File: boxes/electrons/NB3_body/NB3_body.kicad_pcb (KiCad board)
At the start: 2 copper layers, 200 x 199.5 mm, 21 parts, among them J1 Conn_01x02_Male, J2 Conn_01x02_Male, J3 Conn_01x02_Male, J4 Conn_01x02_Male, J5 Conn_01x04_Male, J6 Conn_01x02_Male

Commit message: Work on NB3_body PCB...
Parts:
- removed C3, C4, C5: 10uF, Capacitor_SMD:C_0805_2012Metric
- removed F3, F4, F6: 1.1h2.2t, Fuse:Fuse_0805_2012Metric
- removed F5: 3h5t, Fuse:Fuse_2920_7451Metric
- added J10: Conn_01x03_Female, Connector_PinHeader_2.54mm:PinHeader_1x03_P2.54mm_Vertical_SMD_Pin1Right, F.Cu at (107.5, 36.0)
- added J11: Conn_02x10_Odd_Even, Connector_PinHeader_2.54mm:PinHeader_2x10_P2.54mm_Vertical_SMD, F.Cu at (169.0, 58.5)
- added J12: Conn_01x04_Male, Connector_PinHeader_2.54mm:PinHeader_1x04_P2.54mm_Vertical_SMD_Pin1Right, F.Cu at (167.5, 74.0)
- added J7: Socket_SM06B-SRSS-TB, NB3_body:Socket_SM06B-SRSS-TB, F.Cu at (26.5, 195.0)
- added J8: Socket_SM06B-SRSS-TB, NB3_body:Socket_SM06B-SRSS-TB, F.Cu at (222.5, 196.0)
- added J9: Conn_01x03_Female, Connector_PinHeader_2.54mm:PinHeader_1x03_P2.54mm_Vertical_SMD_Pin1Right, F.Cu at (141.5, 36.0)
- J1, J2: value Conn_01x02_Male -> Conn_01x03_Female; footprint Connector_PinHeader_2.54mm:PinHeader_1x02_P2.54mm_Vertical_SMD_Pin1Right -> Connector_PinHeader_2.54mm:PinHeader_1x03_P2.54mm_Vertical_SMD_Pin1Right
- J3, J4, J6: value Conn_01x02_Male -> Conn_01x10_Male; footprint Connector_PinHeader_2.54mm:PinHeader_1x02_P2.54mm_Vertical_SMD_Pin1Right -> Connector_PinHeader_2.54mm:PinHeader_1x10_P2.54mm_Vertical_SMD_Pin1Right
- J5: value Conn_01x04_Male -> Conn_01x10_Male; footprint Connector_PinHeader_2.54mm:PinHeader_1x04_P2.54mm_Vertical_SMD_Pin1Right -> Connector_PinHeader_2.54mm:PinHeader_1x10_P2.54mm_Vertical_SMD_Pin1Right
- moved J2 127.7 mm to (163.5, 34.5), turned to 90 degrees
- moved J1 124.2 mm to (87.0, 34.0), turned to 90 degrees
- moved J3 86.6 mm to (67.5, 88.0), turned to 90 degrees
- moved H1 84.1 mm to (93.5, 58.0)
- moved C2 83.4 mm to (109.5, 71.5)
- moved J4 81.8 mm to (181.5, 88.0), turned to 90 degrees
- moved H2 79.8 mm to (136.5, 58.0)
- moved C1 78.1 mm to (117.5, 71.5)
- moved F1 73.2 mm to (117.5, 78.0)
- moved F2 72.2 mm to (109.5, 78.0)
- moved H3 62.2 mm to (93.5, 96.0)
- moved H4 52.8 mm to (136.5, 96.0)
- moved J5 43.0 mm to (76.5, 163.0), turned to 90 degrees
- moved J6 35.8 mm to (172.5, 163.0), turned to -90 degrees
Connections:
- C1 pad 1: +5V -> unconnected-(C1-Pad1)
- C1 pad 2: GND -> unconnected-(C1-Pad2)
- C2 pad 1: +5V -> unconnected-(C2-Pad1)
- C2 pad 2: GND -> unconnected-(C2-Pad2)
- F1 pad 1: Net-(F1-Pad1) -> unconnected-(F1-Pad1)
- F1 pad 2: +5V -> unconnected-(F1-Pad2)
- F2 pad 1: Net-(F2-Pad1) -> unconnected-(F2-Pad1)
- F2 pad 2: +5V -> unconnected-(F2-Pad2)
- J1 pad 1: GND -> unconnected-(J1-Pad1)
- J1 pad 2: Net-(F1-Pad1) -> unconnected-(J1-Pad2)
- J2 pad 1: GND -> unconnected-(J2-Pad1)
- J2 pad 2: Net-(F2-Pad1) -> unconnected-(J2-Pad2)
- J3 pad 1: GND -> unconnected-(J3-Pad1)
- J3 pad 2: Net-(F3-Pad1) -> unconnected-(J3-Pad2)
- J4 pad 1: GND -> unconnected-(J4-Pad1)
- J4 pad 2: Net-(F4-Pad1) -> unconnected-(J4-Pad2)
- J5 pad 1: GND -> unconnected-(J5-Pad1)
- J5 pad 2: GND -> unconnected-(J5-Pad2)
- J5 pad 3: Net-(F5-Pad1) -> unconnected-(J5-Pad3)
- J5 pad 4: Net-(F5-Pad1) -> unconnected-(J5-Pad4)
- J6 pad 1: GND -> unconnected-(J6-Pad1)
- J6 pad 2: Net-(F6-Pad1) -> unconnected-(J6-Pad2)
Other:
- outline, holes or cut-outs redrawn

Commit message: Work on NB£_body PCB layout
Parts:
- added J13: Connector_B6B-ZR-SM4-GW-TF(LF)(SN), NB3_body:Connector_B6B-ZR-SM4-GW-TF(LF)(SN), F.Cu at (31.5, 195.0)
- added J14: Connector_B6B-ZR-SM4-GW-TF(LF)(SN), NB3_body:Connector_B6B-ZR-SM4-GW-TF(LF)(SN), F.Cu at (216.5, 195.0)
- J1, J2: value Conn_01x03_Female -> Conn_02x05_Counter_Clockwise; footprint Connector_PinHeader_2.54mm:PinHeader_1x03_P2.54mm_Vertical_SMD_Pin1Right -> Connector_PinSocket_2.54mm:PinSocket_2x05_P2.54mm_Vertical_SMD
- J10: value Conn_01x03_Female -> Conn_02x03_Top_Bottom; footprint Connector_PinHeader_2.54mm:PinHeader_1x03_P2.54mm_Vertical_SMD_Pin1Right -> Connector_PinHeader_2.54mm:PinHeader_2x03_P2.54mm_Vertical_SMD
- J11: value Conn_02x10_Odd_Even -> Conn_02x03_Top_Bottom; footprint Connector_PinHeader_2.54mm:PinHeader_2x10_P2.54mm_Vertical_SMD -> Connector_PinHeader_2.54mm:PinHeader_2x03_P2.54mm_Vertical_SMD
- J12: value Conn_01x04_Male -> Conn_02x03_Top_Bottom; footprint Connector_PinHeader_2.54mm:PinHeader_1x04_P2.54mm_Vertical_SMD_Pin1Right -> Connector_PinHeader_2.54mm:PinHeader_2x03_P2.54mm_Vertical_SMD
- J3, J4, J5, J6: value Conn_01x10_Male -> Conn_02x05_Counter_Clockwise; footprint Connector_PinHeader_2.54mm:PinHeader_1x10_P2.54mm_Vertical_SMD_Pin1Right -> Connector_PinSocket_2.54mm:PinSocket_2x05_P2.54mm_Vertical_SMD
- J7, J8: value Socket_SM06B-SRSS-TB -> Conn_02x05_Counter_Clockwise; footprint NB3_body:Socket_SM06B-SRSS-TB -> Connector_PinSocket_2.54mm:PinSocket_2x05_P2.54mm_Vertical_SMD
- J9: value Conn_01x03_Female -> Connector_S4B-PH-SM4-TB(LF)(SN); footprint Connector_PinHeader_2.54mm:PinHeader_1x03_P2.54mm_Vertical_SMD_Pin1Right -> NB3_body:Connector_S4B-PH-SM4-TB(LF)(SN)
- moved J7 191.0 mm to (158.5, 57.0), turned to 0 degrees
- moved J11 165.6 mm to (47.5, 171.0), turned to 0 degrees
- moved J8 117.9 mm to (158.5, 97.0), turned to 0 degrees
- moved J12 102.5 mm to (203.5, 170.0)
- moved J9 44.4 mm to (158.5, 77.0), turned to 90 degrees
- moved J10 17.1 mm to (124.5, 38.0), turned to 0 degrees
- moved J6 7.91 mm to (165.0, 160.5), turned to 90 degrees
- moved J4 7.70 mm to (174.0, 86.2)
- moved H1 3.00 mm to (90.5, 58.0)
- moved H2 3.00 mm to (133.5, 58.0)
- moved H3 3.00 mm to (90.5, 96.0)
- moved H4 3.00 mm to (133.5, 96.0)
- moved J2 2.00 mm to (161.5, 34.5)
- moved J3 2.00 mm to (67.5, 86.0)
- moved J5 2.00 mm to (76.5, 161.0)
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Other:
- board text added: "5v rA rB rC rD 0v rE rF rG rH"

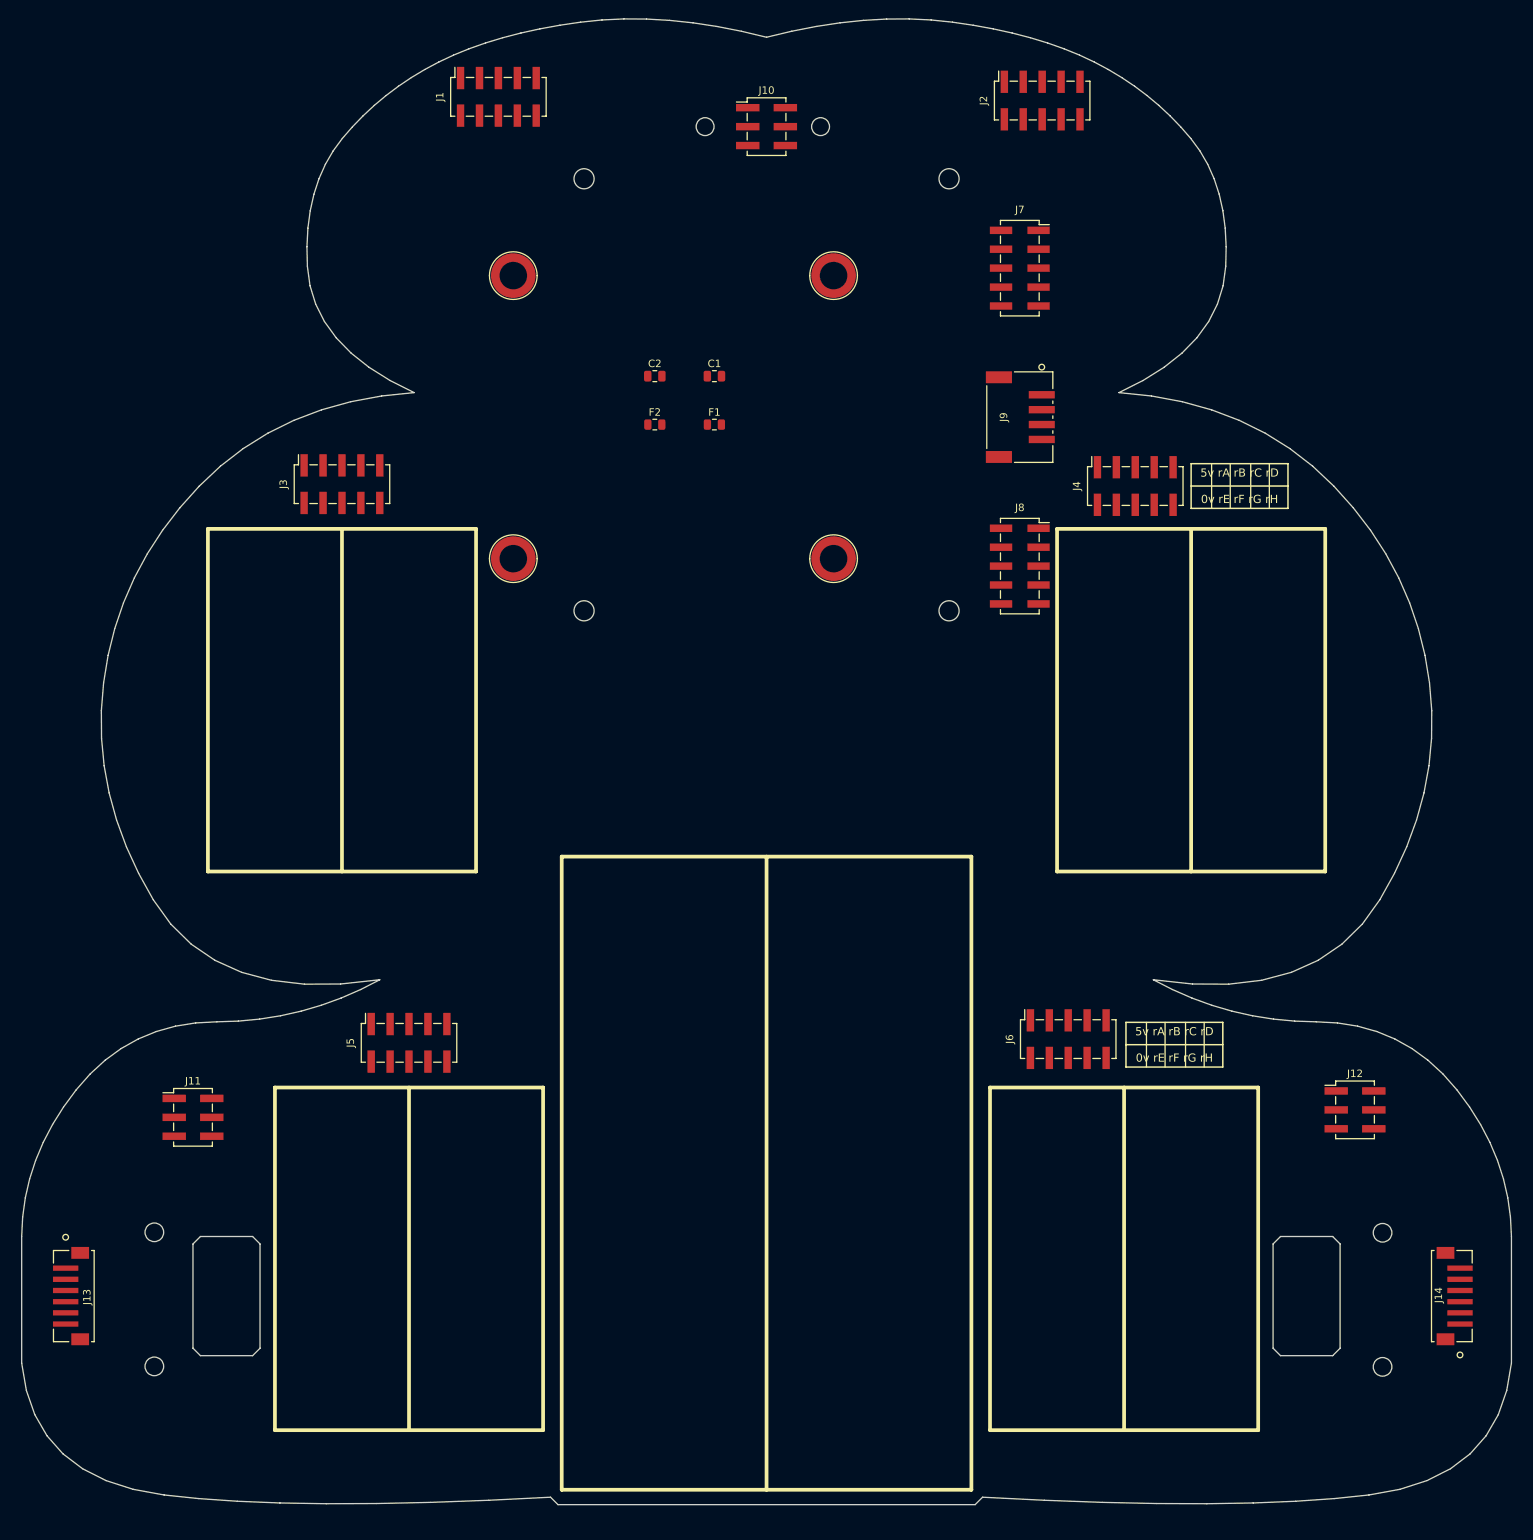
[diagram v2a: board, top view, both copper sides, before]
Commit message: Work on NB3_body routing
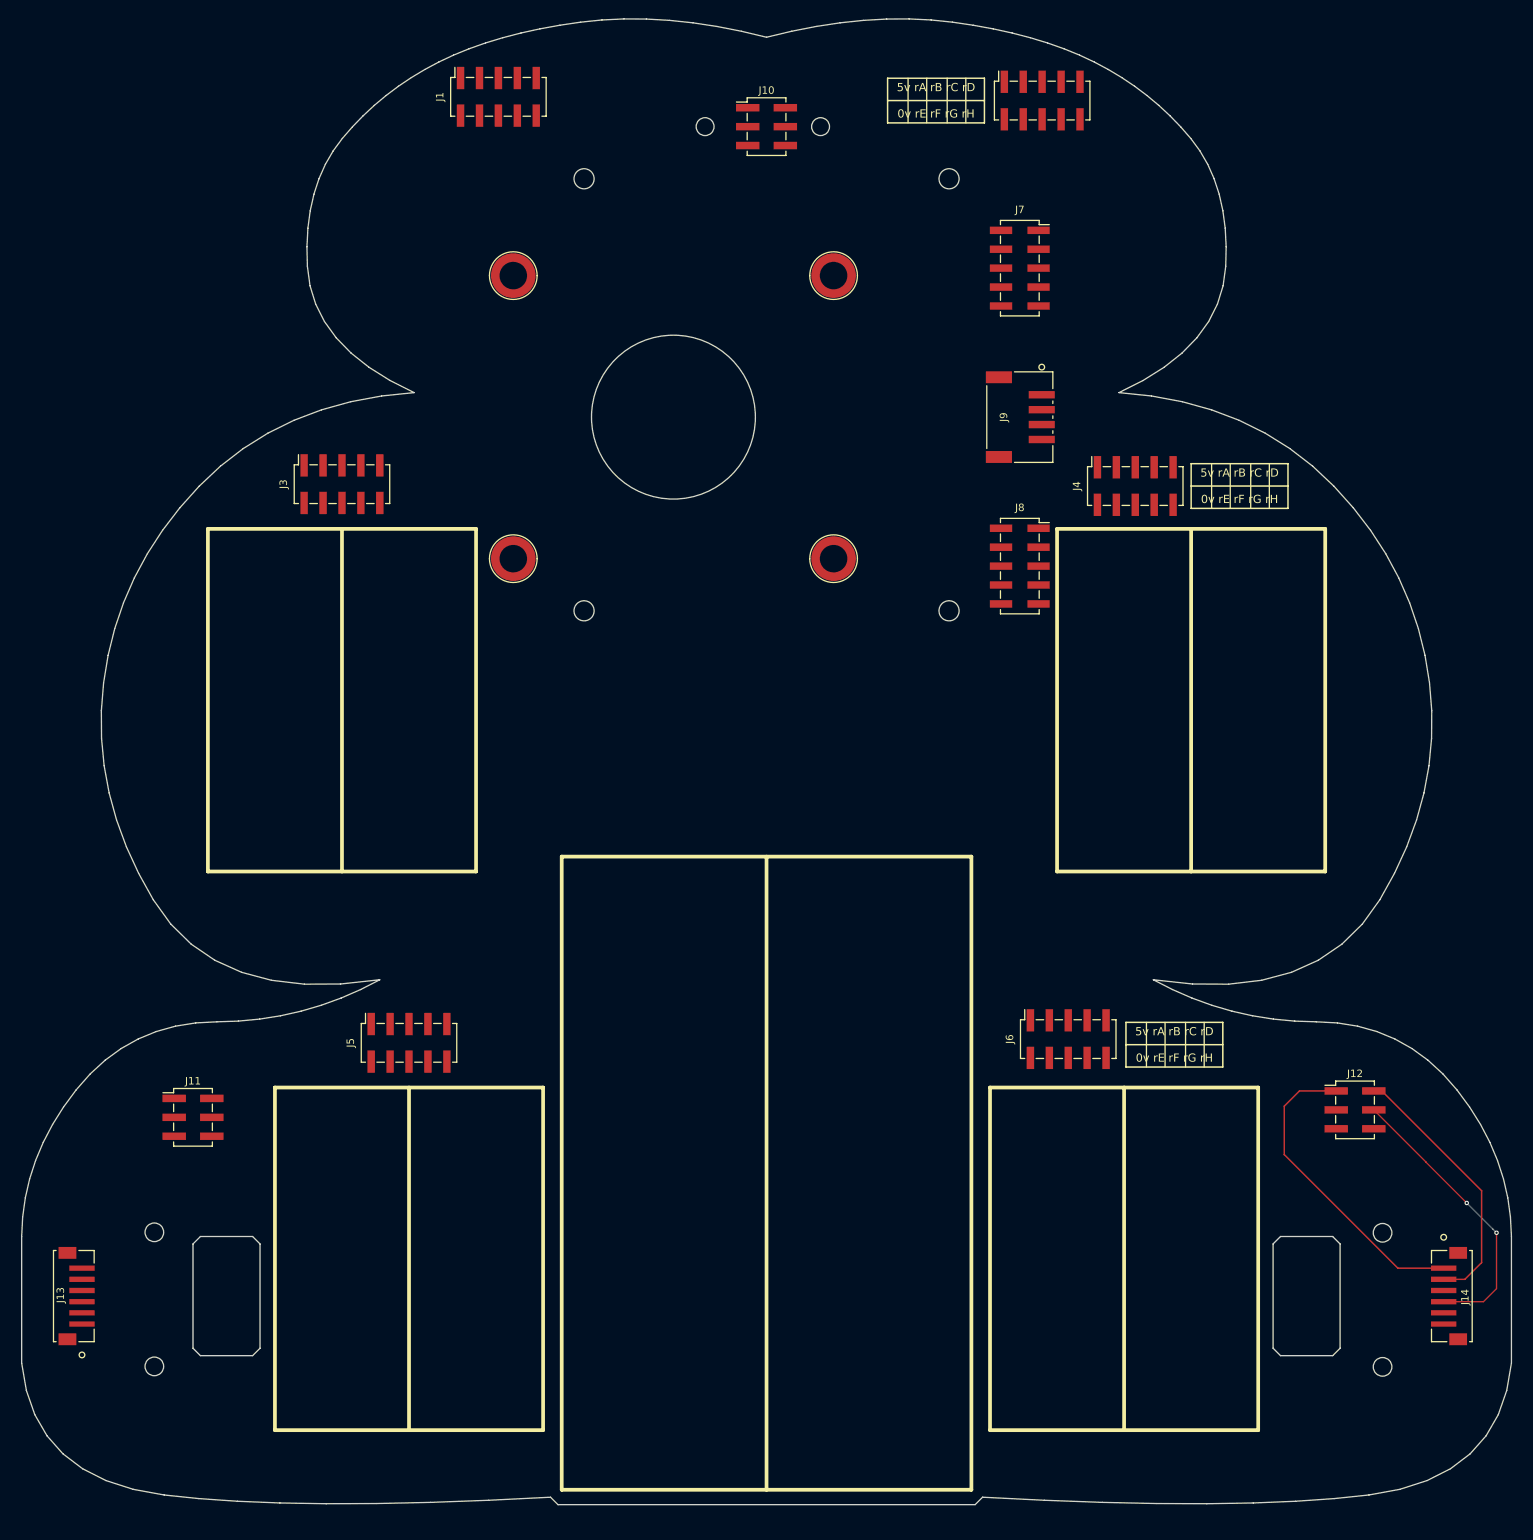
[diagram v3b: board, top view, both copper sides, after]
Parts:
- removed C1, C2: 10uF, Capacitor_SMD:C_0805_2012Metric
- removed F1, F2: 1.1h2.2t, Fuse:Fuse_0805_2012Metric
- J13, J14: value Connector_B6B-ZR-SM4-GW-TF(LF)(SN) -> JST ZH 6-way Socket
- J9: value Connector_S4B-PH-SM4-TB(LF)(SN) -> JST SH 4-way Socket
- turned J13 to 90 degrees
- turned J14 to -90 degrees
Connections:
- J1 pad 1: unconnected-(J1-Pad1) -> +5V
- J1 pad 10: unconnected-(J1-Pad10) -> GND
- J1 pad 2: unconnected-(J1-Pad2) -> /LA
- J1 pad 3: unconnected-(J1-Pad3) -> /LB
- J1 pad 4: unconnected-(J1-Pad4) -> /LC
- J1 pad 5: unconnected-(J1-Pad5) -> /LD
- J1 pad 6: unconnected-(J1-Pad6) -> /LH
- J1 pad 7: unconnected-(J1-Pad7) -> /LG
- J1 pad 8: unconnected-(J1-Pad8) -> /LF
- J1 pad 9: unconnected-(J1-Pad9) -> /LE
- J10 pad 1: unconnected-(J10-Pad1) -> GND
- J10 pad 2: unconnected-(J10-Pad2) -> +5V
- J10 pad 3: unconnected-(J10-Pad3) -> /LH
- J10 pad 4: unconnected-(J10-Pad4) -> GND
- J10 pad 5: unconnected-(J10-Pad5) -> +5V
- J10 pad 6: unconnected-(J10-Pad6) -> /RH
- J11 pad 1: unconnected-(J11-Pad1) -> /LM+
- J11 pad 2: unconnected-(J11-Pad2) -> /LE+
- J11 pad 3: unconnected-(J11-Pad3) -> /LE A
- J11 pad 4: unconnected-(J11-Pad4) -> /LE B
- J11 pad 5: unconnected-(J11-Pad5) -> /LE-
- J11 pad 6: unconnected-(J11-Pad6) -> /LM-
- J12 pad 1: unconnected-(J12-Pad1) -> /RM+
- J12 pad 2: unconnected-(J12-Pad2) -> /RE+
- J12 pad 3: unconnected-(J12-Pad3) -> /RE A
- J12 pad 4: unconnected-(J12-Pad4) -> /RE B
- J12 pad 5: unconnected-(J12-Pad5) -> /RE-
- J12 pad 6: unconnected-(J12-Pad6) -> /RM-
- J13 pad 1: unconnected-(J13-Pad1) -> /LM+
- J13 pad 2: unconnected-(J13-Pad2) -> /LE+
- J13 pad 3: unconnected-(J13-Pad3) -> /LE A
- J13 pad 4: unconnected-(J13-Pad4) -> /LE B
- J13 pad 5: unconnected-(J13-Pad5) -> /LE-
- J13 pad 6: unconnected-(J13-Pad6) -> /LM-
- J14 pad 1: unconnected-(J14-Pad1) -> /RM+
- J14 pad 2: unconnected-(J14-Pad2) -> /RE+
- J14 pad 3: unconnected-(J14-Pad3) -> /RE A
- J14 pad 4: unconnected-(J14-Pad4) -> /RE B
- J14 pad 5: unconnected-(J14-Pad5) -> /RE-
- J14 pad 6: unconnected-(J14-Pad6) -> /RM-
- J2 pad 1: unconnected-(J2-Pad1) -> +5V
- J2 pad 10: unconnected-(J2-Pad10) -> GND
- J2 pad 2: unconnected-(J2-Pad2) -> /RA
- J2 pad 3: unconnected-(J2-Pad3) -> /RB
- J2 pad 4: unconnected-(J2-Pad4) -> /RC
- J2 pad 5: unconnected-(J2-Pad5) -> /RD
- J2 pad 6: unconnected-(J2-Pad6) -> /RH
- J2 pad 7: unconnected-(J2-Pad7) -> /RG
- J2 pad 8: unconnected-(J2-Pad8) -> /RF
- J2 pad 9: unconnected-(J2-Pad9) -> /RE
- J3 pad 1: unconnected-(J3-Pad1) -> +5V
- J3 pad 10: unconnected-(J3-Pad10) -> GND
- J3 pad 2: unconnected-(J3-Pad2) -> /LA
- J3 pad 3: unconnected-(J3-Pad3) -> /LB
- J3 pad 4: unconnected-(J3-Pad4) -> /LC
- J3 pad 5: unconnected-(J3-Pad5) -> /LD
- J3 pad 6: unconnected-(J3-Pad6) -> /LH
- J3 pad 7: unconnected-(J3-Pad7) -> /LG
- J3 pad 8: unconnected-(J3-Pad8) -> /LF
- J3 pad 9: unconnected-(J3-Pad9) -> /LE
- J4 pad 1: unconnected-(J4-Pad1) -> +5V
- J4 pad 10: unconnected-(J4-Pad10) -> GND
- J4 pad 2: unconnected-(J4-Pad2) -> /RA
- J4 pad 3: unconnected-(J4-Pad3) -> /RB
- J4 pad 4: unconnected-(J4-Pad4) -> /RC
- J4 pad 5: unconnected-(J4-Pad5) -> /RD
- J4 pad 6: unconnected-(J4-Pad6) -> /RH
- J4 pad 7: unconnected-(J4-Pad7) -> /RG
- J4 pad 8: unconnected-(J4-Pad8) -> /RF
- J4 pad 9: unconnected-(J4-Pad9) -> /RE
- J5 pad 1: unconnected-(J5-Pad1) -> +5V
- J5 pad 10: unconnected-(J5-Pad10) -> GND
- J5 pad 2: unconnected-(J5-Pad2) -> /LA
- J5 pad 3: unconnected-(J5-Pad3) -> /LB
- J5 pad 4: unconnected-(J5-Pad4) -> /LC
- J5 pad 5: unconnected-(J5-Pad5) -> /LD
- J5 pad 6: unconnected-(J5-Pad6) -> /LH
- J5 pad 7: unconnected-(J5-Pad7) -> /LG
- J5 pad 8: unconnected-(J5-Pad8) -> /LF
- J5 pad 9: unconnected-(J5-Pad9) -> /LE
- J6 pad 1: unconnected-(J6-Pad1) -> +5V
- J6 pad 10: unconnected-(J6-Pad10) -> GND
- J6 pad 2: unconnected-(J6-Pad2) -> /RA
- J6 pad 3: unconnected-(J6-Pad3) -> /RB
- J6 pad 4: unconnected-(J6-Pad4) -> /RC
- J6 pad 5: unconnected-(J6-Pad5) -> /RD
- J6 pad 6: unconnected-(J6-Pad6) -> /RH
- J6 pad 7: unconnected-(J6-Pad7) -> /RG
- J6 pad 8: unconnected-(J6-Pad8) -> /RF
- J6 pad 9: unconnected-(J6-Pad9) -> /RE
- J7 pad 1: unconnected-(J7-Pad1) -> +5V
- J7 pad 10: unconnected-(J7-Pad10) -> GND
- J7 pad 2: unconnected-(J7-Pad2) -> +5V
- J7 pad 3: unconnected-(J7-Pad3) -> /LA
- J7 pad 4: unconnected-(J7-Pad4) -> /LB
- J7 pad 5: unconnected-(J7-Pad5) -> /LC
- J7 pad 6: unconnected-(J7-Pad6) -> /RC
- J7 pad 7: unconnected-(J7-Pad7) -> /RB
- J7 pad 8: unconnected-(J7-Pad8) -> /RA
- J7 pad 9: unconnected-(J7-Pad9) -> GND
- J8 pad 1: unconnected-(J8-Pad1) -> /LD
- J8 pad 10: unconnected-(J8-Pad10) -> /RD
- J8 pad 2: unconnected-(J8-Pad2) -> /LE
- J8 pad 3: unconnected-(J8-Pad3) -> /LF
- J8 pad 4: unconnected-(J8-Pad4) -> /LG
- J8 pad 5: unconnected-(J8-Pad5) -> /LH
- J8 pad 6: unconnected-(J8-Pad6) -> /RH
- J8 pad 7: unconnected-(J8-Pad7) -> /RG
- J8 pad 8: unconnected-(J8-Pad8) -> /RF
- J8 pad 9: unconnected-(J8-Pad9) -> /RE
- J9 pad 1: unconnected-(J9-Pad1) -> +5V
- J9 pad 2: unconnected-(J9-Pad2) -> +5V
- J9 pad 3: unconnected-(J9-Pad3) -> GND
- J9 pad 4: unconnected-(J9-Pad4) -> GND
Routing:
- net /RM+: track 0.00 -> 42.0 mm
- net /RE B: track 0.00 -> 38.6 mm, vias 0 -> 2
- net /RE+: track 0.00 -> 35.7 mm
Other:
- outline, holes or cut-outs redrawn
